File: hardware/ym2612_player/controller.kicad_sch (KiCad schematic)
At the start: 23 parts, among them J1 Spare GPIO (not fitted), U2 Pimoroni Pico Plus 2

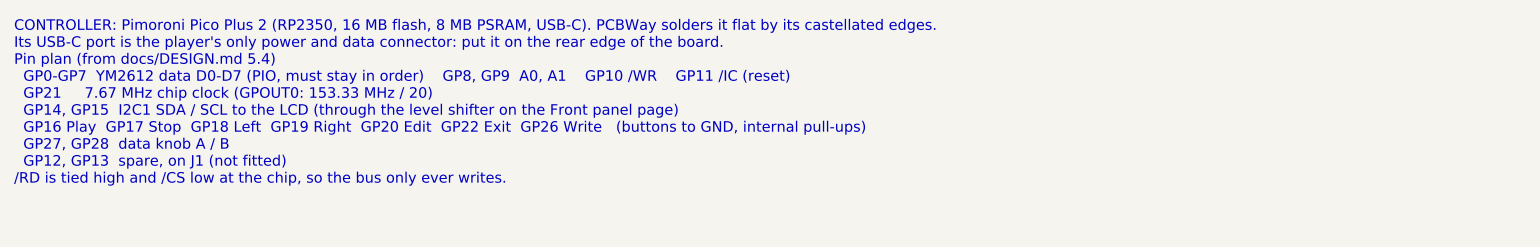
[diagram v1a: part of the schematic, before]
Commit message: Mount the Pico Plus 2 on sockets, pick the window LED, tidy labels
The Pico Plus 2 has flash, PSRAM and a connector on its underside, so it
can't be soldered flat. It now plugs into two 1x20 female sockets in the
standard Pico hole pattern; the BOM gains the sockets and the headers for
the module. Tracks around it are re-routed. DRC in KiCad 10: 0 errors,
0 unconnected, matches the schematic.

Window LEDs: Lumimax LED3WAW (3 mm warm white). New tools/silk.py moves
part labels clear of pads and each other; values move to the fab layer.

Co-Authored-By: Claude Opus 5.5 (1M context) <noreply@anthropic.com>
Claude-Session: https://claude.ai/code/session_01JeM5NcWqyQVA3DixJkw6Wg
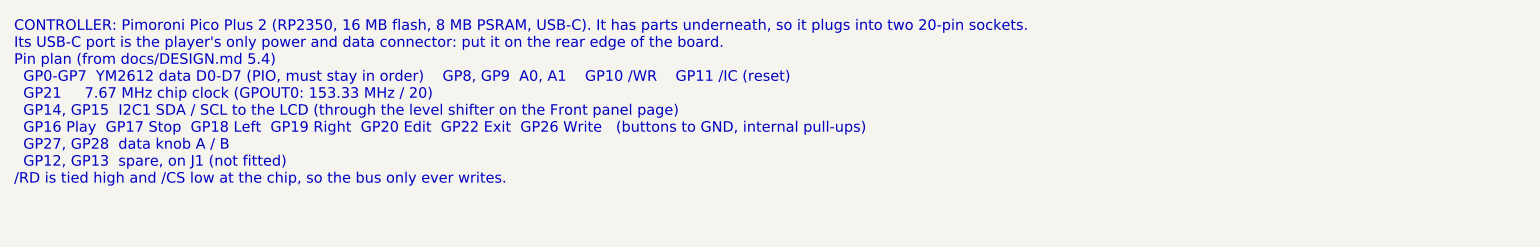
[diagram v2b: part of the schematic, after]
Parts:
- U2: footprint ym2612:Pimoroni_PicoPlus2_SMD -> ym2612:Pimoroni_PicoPlus2_Socketed; Spec Pimoroni Pico Plus 2, Digi-Key PIM724, soldered flat by its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 -> Pimoroni Pico Plus 2, Digi-Key PIM724, with 2x 20-pin male 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
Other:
- note added: "CONTROLLER: Pimoroni Pico Plus 2 (RP2350, 16 MB flash, 8 MB PSRAM, USB-C). It has parts underneath, so it plugs into two 20-pin sockets. Its USB-C port is the player's only power and data connector: put it on the rear edge of the board. Pin plan (from docs/DESIGN.md 5.4) GP0-GP7 YM2612 data D0-D7 (PIO, must stay in order) GP8, GP9 A0, A1 GP10 /WR GP11 /IC (reset) GP21 7.67 MHz chip clock (GPOUT0: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"
- note removed: "CONTROLLER: Pimoroni Pico Plus 2 (RP2350, 16 MB flash, 8 MB PSRAM, USB-C). PCBWay solders it flat by its castellated edges. Its USB-C port is the player's only power and data connector: put it on the rear edge of the board. Pin plan (from docs/DESIGN.md 5.4) GP0-GP7 YM2612 data D0-D7 (PIO, must stay in order) GP8, GP9 A0, A1 GP10 /WR GP11 /IC (reset) GP21 7.67 MHz chip clock (GPOUT0: 153.33 MHz /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"
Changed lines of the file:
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@@
       (effects (font (size 1.27 1.27)))
     )
-    (property "Footprint" "ym2612:Pimoroni_PicoPlus2_SMD" (at 165.1 139.7 0)
+    (property "Footprint" "ym2612:Pimoroni_PicoPlus2_Socketed" (at 165.1 139.7 0)
       (effects (font (size 1.27 1.27)) hide)
     )
@@
       (effects (font (size 1.27 1.27)) hide)
     )
-    (property "Spec" "Pimoroni Pico Plus 2, Digi-Key PIM724, soldered flat by its castellated edges" (at 165.1 139.7 0)
+    (property "Spec" "Pimoroni Pico Plus 2, Digi-Key PIM724, with 2x 20-pin male headers soldered on, plugged into sockets U2-SKT" (at 165.1 139.7 0)
       (effects (font (size 1.27 1.27)) hide)
     )
@@
     )
   )
-  (text "CONTROLLER: Pimoroni Pico Plus 2 (RP2350, 16 MB flash, 8 MB PSRAM, USB-C). PCBWay solders it flat by its castellated edges.\nIts USB-C port is the player's only power and data connector: put it on the rear edge of the board.\nPin plan (from docs/DESIGN.md 5.4)\n  GP0-GP7  YM2612 data D0-D7 (PIO, must stay in order)    GP8, GP9  A0, A1    GP10 /WR    GP11 /IC (reset)\n  GP21     7.67 MHz chip clock (GPOUT0: 153.33 MHz / 20)\n  GP14, GP15  I2C1 SDA / SCL to the LCD (through the level shifter on the Front panel page)\n  GP16 Play  GP17 Stop  GP18 Left  GP19 Right  GP20 Edit  GP22 Exit  GP26 Write   (buttons to GND, internal pull-ups)\n  GP27, GP28  data knob A / B\n  GP12, GP13  spare, on J1 (not fitted)\n/RD is tied high and /CS low at the chip, so the bus only ever writes." (at 25.4 25.4 0)
+  (text "CONTROLLER: Pimoroni Pico Plus 2 (RP2350, 16 MB flash, 8 MB PSRAM, USB-C). It has parts underneath, so it plugs into two 20-pin sockets.\nIts USB-C port is the player's only power and data connector: put it on the rear edge of the board.\nPin plan (from docs/DESIGN.md 5.4)\n  GP0-GP7  YM2612 data D0-D7 (PIO, must stay in order)    GP8, GP9  A0, A1    GP10 /WR    GP11 /IC (reset)\n  GP21     7.67 MHz chip clock (GPOUT0: 153.33 MHz / 20)\n  GP14, GP15  I2C1 SDA / SCL to the LCD (through the level shifter on the Front panel page)\n  GP16 Play  GP17 Stop  GP18 Left  GP19 Right  GP20 Edit  GP22 Exit  GP26 Write   (buttons to GND, internal pull-ups)\n  GP27, GP28  data knob A / B\n  GP12, GP13  spare, on J1 (not fitted)\n/RD is tied high and /CS low at the chip, so the bus only ever writes." (at 25.4 25.4 0)
     (effects (font (size 1.5 1.5)) (justify left top))
   )

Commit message: Apply the Rev A fix register: decoupling, single ground, A.VCC filter, TPA6132A2
Schematic
- YM2612 A.VCC (pin 22) gets its own 10 ohm + 220 uF + 100 nF filter.
- /IC, A0, A1 pull-downs 10k -> 4.7k (RP2350 erratum E9).
- Headphone amp: NJM4556A replaced by a TPA6132A2 at -6 dB, no output caps,
  enabled by GP12 (HP_EN, 4.7k pull-down) so power-up doesn't pop.
- 47 uF electrolytic damps the L1/C4 resonance before the LP5907.
- GNDA merged into GND; NT1 removed. Four M3 holes for the LCD standoffs.
- Ferrite label 220R@100MHz to match BLM18PG221SN1D; C15/C22 spec X7R 50V;
  LED lead note for PCBWay.
- Pico Plus 2 and its headers marked do-not-fit (Joey supplies them);
  sockets are Sullins PPTC201LFBN-RC.

Layout
- Decoupling caps placed at the pin they serve (design.NEAR), 2-7 mm instead
  of 16-70 mm.
- One solid GND plane on both layers plus 332 stitching vias (tools/stitch.py).
- J6 moved out from under the LCD backpack; encoder moved below the LCD so
  the knob clears it.
- Re-routed with Freerouting; KiCad 7 DRC: 0 errors, 0 unconnected.

Co-Authored-By: Claude Opus 5.5 (1M context) <noreply@anthropic.com>
Claude-Session: https://claude.ai/code/session_01T6y8roX1LzS9uTuKVQBe9X
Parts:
- removed C7: 10uF, Capacitor_SMD:C_0805_2012Metric, symbol Device:C
- removed C8: 100nF, Capacitor_SMD:C_0603_1608Metric, symbol Device:C
- removed U2: Pimoroni Pico Plus 2, ym2612:Pimoroni_PicoPlus2_Socketed, symbol ym2612:PicoPlus2
- added TP13: YM_CLK, TestPoint:TestPoint_Pad_D1.5mm, symbol Connector:TestPoint
- added TP14, TP15: GND, TestPoint:TestPoint_Pad_D1.5mm, symbol Connector:TestPoint
- C8: renamed from R2; value 10k -> 10uF; footprint Resistor_SMD:R_0603_1608Metric -> Capacitor_SMD:C_0805_2012Metric; symbol Device:R -> Device:C; Spec 1%, 0603 -> X5R, 10V, 0805
- C9: renamed from R3; value 10k -> 100nF; footprint Resistor_SMD:R_0603_1608Metric -> Capacitor_SMD:C_0603_1608Metric; symbol Device:R -> Device:C; Spec 1%, 0603 -> X7R, 16V
- J1: renamed from TP3; value D2 -> Spare GPIO (not fitted); footprint TestPoint:TestPoint_Pad_D1.5mm -> Connector_PinHeader_2.54mm:PinHeader_1x04_P2.54mm_Vertical; symbol Connector:TestPoint -> Connector_Generic:Conn_01x04; now not fitted
- R2: renamed from J1; value Spare GPIO (not fitted) -> 4.7k; footprint Connector_PinHeader_2.54mm:PinHeader_1x04_P2.54mm_Vertical -> Resistor_SMD:R_0603_1608Metric; symbol Connector_Generic:Conn_01x04 -> Device:R; Spec (none) -> 1%, 0603; now fitted
- R3: renamed from TP1; value D0 -> 4.7k; footprint TestPoint:TestPoint_Pad_D1.5mm -> Resistor_SMD:R_0603_1608Metric; symbol Connector:TestPoint -> Device:R; Spec (none) -> 1%, 0603
- R4: renamed from TP2; value D1 -> 4.7k; footprint TestPoint:TestPoint_Pad_D1.5mm -> Resistor_SMD:R_0603_1608Metric; symbol Connector:TestPoint -> Device:R; Spec (none) -> 1%, 0603
- TP1: renamed from TP4; value D3 -> D0
- TP10: renamed from TP13; value YM_CLK -> A1
- TP11: renamed from TP14; value GND -> WR
- TP12: renamed from TP15; value GND -> IC
- TP2: renamed from TP5; value D4 -> D1
- TP3: renamed from TP6; value D5 -> D2
- TP4: renamed from TP7; value D6 -> D3
- TP5: renamed from TP8; value D7 -> D4
- TP6: renamed from TP9; value A0 -> D5
- TP7: renamed from TP10; value A1 -> D6
- TP8: renamed from TP11; value WR -> D7
- TP9: renamed from TP12; value IC -> A0
- U2: renamed from R1; value 10k -> Pimoroni Pico Plus 2; footprint Resistor_SMD:R_0603_1608Metric -> ym2612:Pimoroni_PicoPlus2_Socketed; symbol Device:R -> ym2612:PicoPlus2; MPN (none) -> PIM724; Spec 1%, 0603 -> Joey supplies the Pico Plus 2 and solders 2x 20-pin male he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; now not fitted
- renumbered R4 to R1
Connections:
- net SPARE_GP12 is gone; now on net GND: R2.2
- net +3V3: now also C8.1, C9.1, J1.1 (Pin_1), R1.1, U2.36 (3V3); no longer R2.1 (Pin_1), U2.1
- net +5V: now also U2.40 (VBUS)
- net BTN_EDIT: now also U2.26 (GP20)
- net BTN_EXIT: now also U2.29 (GP22)
- net BTN_LEFT: now also U2.24 (GP18)
- net BTN_PLAY: now also U2.21 (GP16)
- net BTN_RIGHT: now also U2.25 (GP19)
- net BTN_STOP: now also U2.22 (GP17)
- net BTN_WRITE: now also U2.31 (GP26)
- net ENC_A: now also U2.32 (GP27)
- net ENC_B: now also U2.34 (GP28)
- net GND: now also J1.4 (Pin_4), R3.2, R4.2, U2.13 (GND), U2.18 (GND), U2.23 (GND), U2.28 (GND), U2.3 (GND), U2.33 (AGND), U2.38 (GND), U2.8 (GND), TP14.1, TP15.1; no longer R1.2, R2.4 (Pin_4), TP11.1, TP12.1
- net I2C_SCL: now also U2.20 (GP15)
- net I2C_SDA: now also U2.19 (GP14)
- net MCU_A0: now also R3.1, TP9.1, U2.11 (GP8); no longer C9.1, TP6.1
- net MCU_A1: now also R4.1, TP10.1, U2.12 (GP9); no longer R1.1, TP7.1
- net MCU_CLK: now also U2.27 (GP21)
- net MCU_D0: now also TP1.1, U2.1 (GP0); no longer R3.1
- net MCU_D1: now also TP2.1, U2.2 (GP1); no longer R4.1
- net MCU_D2: now also TP3.1, U2.4 (GP2); no longer J1.1
- net MCU_D3: now also TP4.1, U2.5 (GP3); no longer TP1.1
- net MCU_D4: now also TP5.1, U2.6 (GP4); no longer TP2.1
- net MCU_D5: now also TP6.1, U2.7 (GP5); no longer TP3.1
- net MCU_D6: now also TP7.1, U2.9 (GP6); no longer TP4.1
- net MCU_D7: now also TP8.1, U2.10 (GP7); no longer TP5.1
- net MCU_IC: now also R2.1, TP12.1, U2.15 (GP11); no longer C8.1, TP9.1
- net MCU_WR: now also R1.2, TP11.1, U2.14 (GP10); no longer TP8.1, U2.2
- net SPARE_GP13: now also J1.3 (Pin_3), U2.17 (GP13); no longer R2.3 (Pin_3)
- net YM_CLK: now also TP13.1; no longer TP10.1
- new net HP_EN: J1.2 (Pin_2), U2.16 (GP12)
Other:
- note added: "Boot-time pulls: until the firmware starts, these hold the YM2612 in reset and keep /WR idle. 4.7k pull-downs: RP2350 erratum E9."
- note removed: "Boot-time pulls: until the firmware starts, these hold the YM2612 in reset and keep /WR idle."
- moved on the sheet: R1, TP1, TP10, TP11, TP12, TP2, TP3, TP4, TP5, TP6, TP7, TP8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

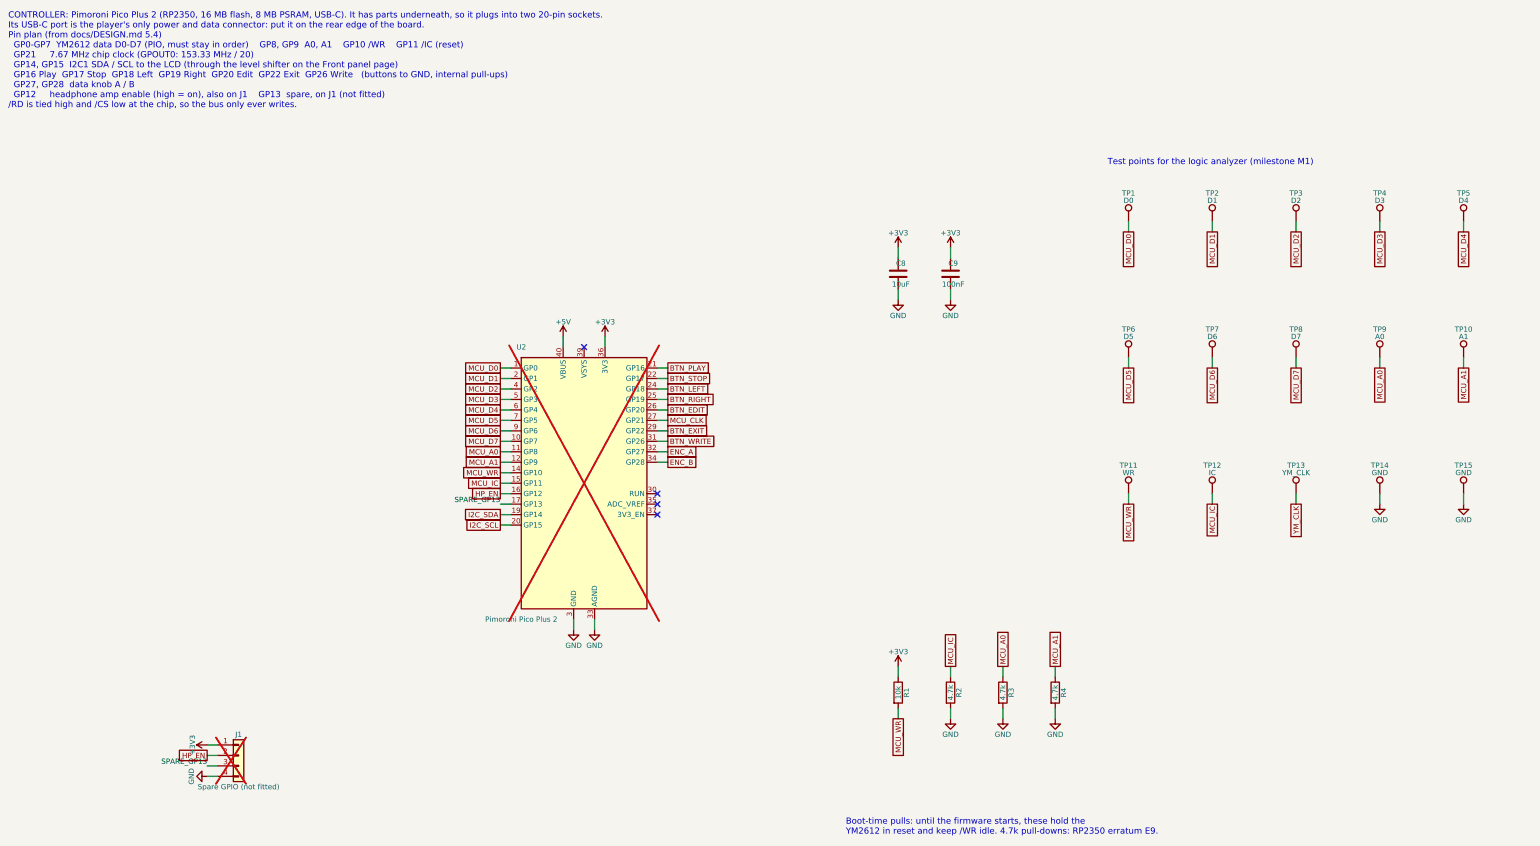
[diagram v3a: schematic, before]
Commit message: Schematic: draw real wires between parts instead of name tags
tools/wires.py routes each page's nets on the 1.27 mm grid around part bodies and text.
Power pins keep power symbols (neighbouring pins share one), signals that leave a page get
one global label, and the netlist check still matches design.py exactly (0 mismatches).
Sound chip and audio pages re-laid out so the wiring reads left to right; title blocks say Rev B.

Co-Authored-By: Claude Opus 5.5 <noreply@anthropic.com>
Claude-Session: https://claude.ai/code/session_01TDTDVidYRoyJdUGgsyVTSw
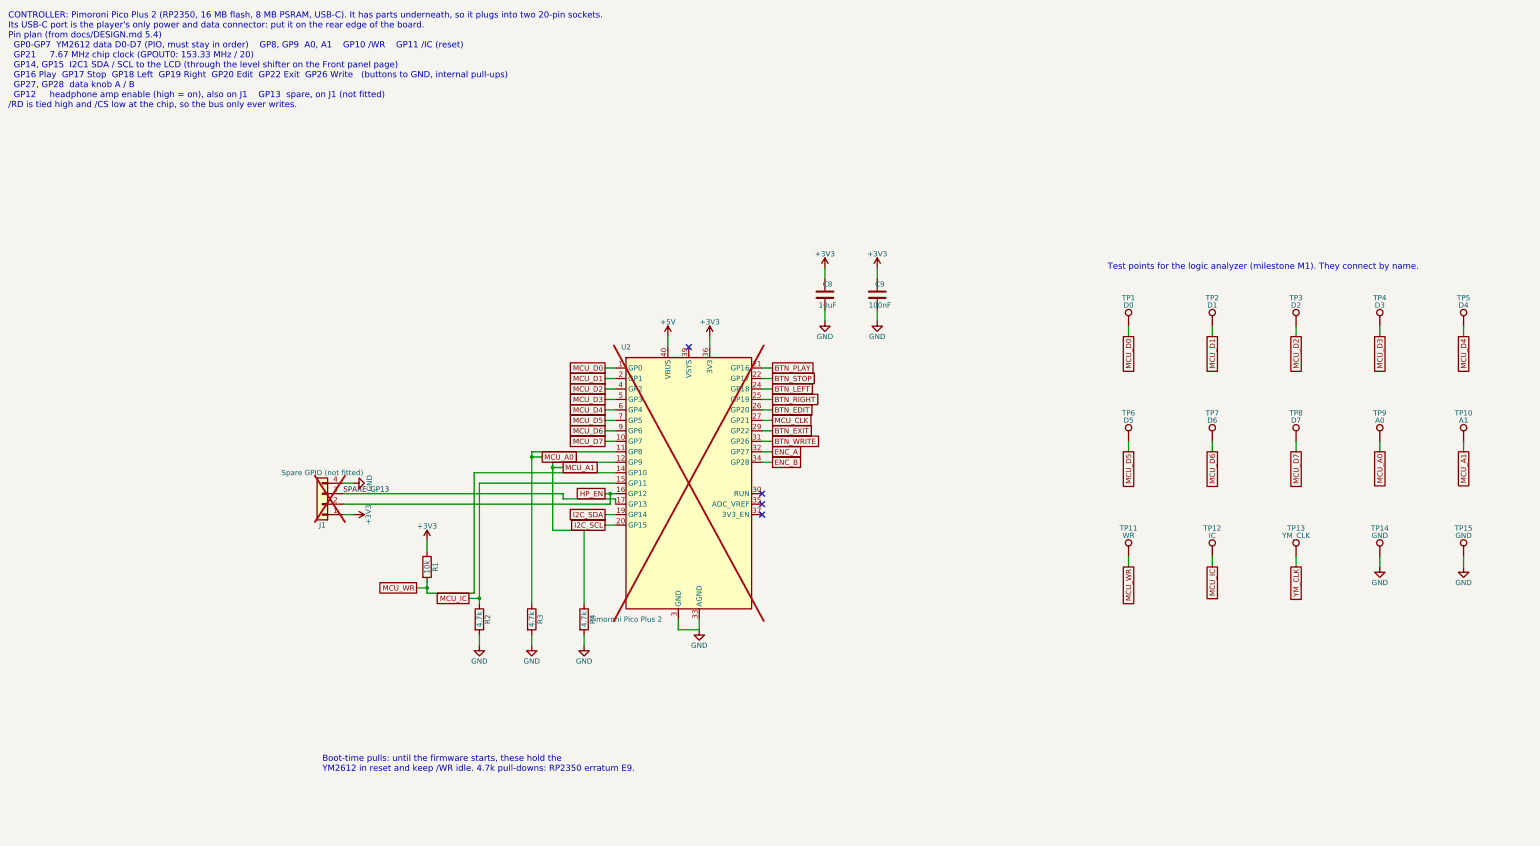
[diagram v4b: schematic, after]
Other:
- note added: "Test points for the logic analyzer (milestone M1). They connect by name."
- note removed: "Test points for the logic analyzer (milestone M1)"
- moved on the sheet: C8, C9, J1, R1, R2, R3, R4, TP1, TP10, TP11, TP12, TP13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
